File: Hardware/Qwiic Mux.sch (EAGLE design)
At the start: 62 parts, among them J2 SMD, J3 SMD, U2 PCA9548A

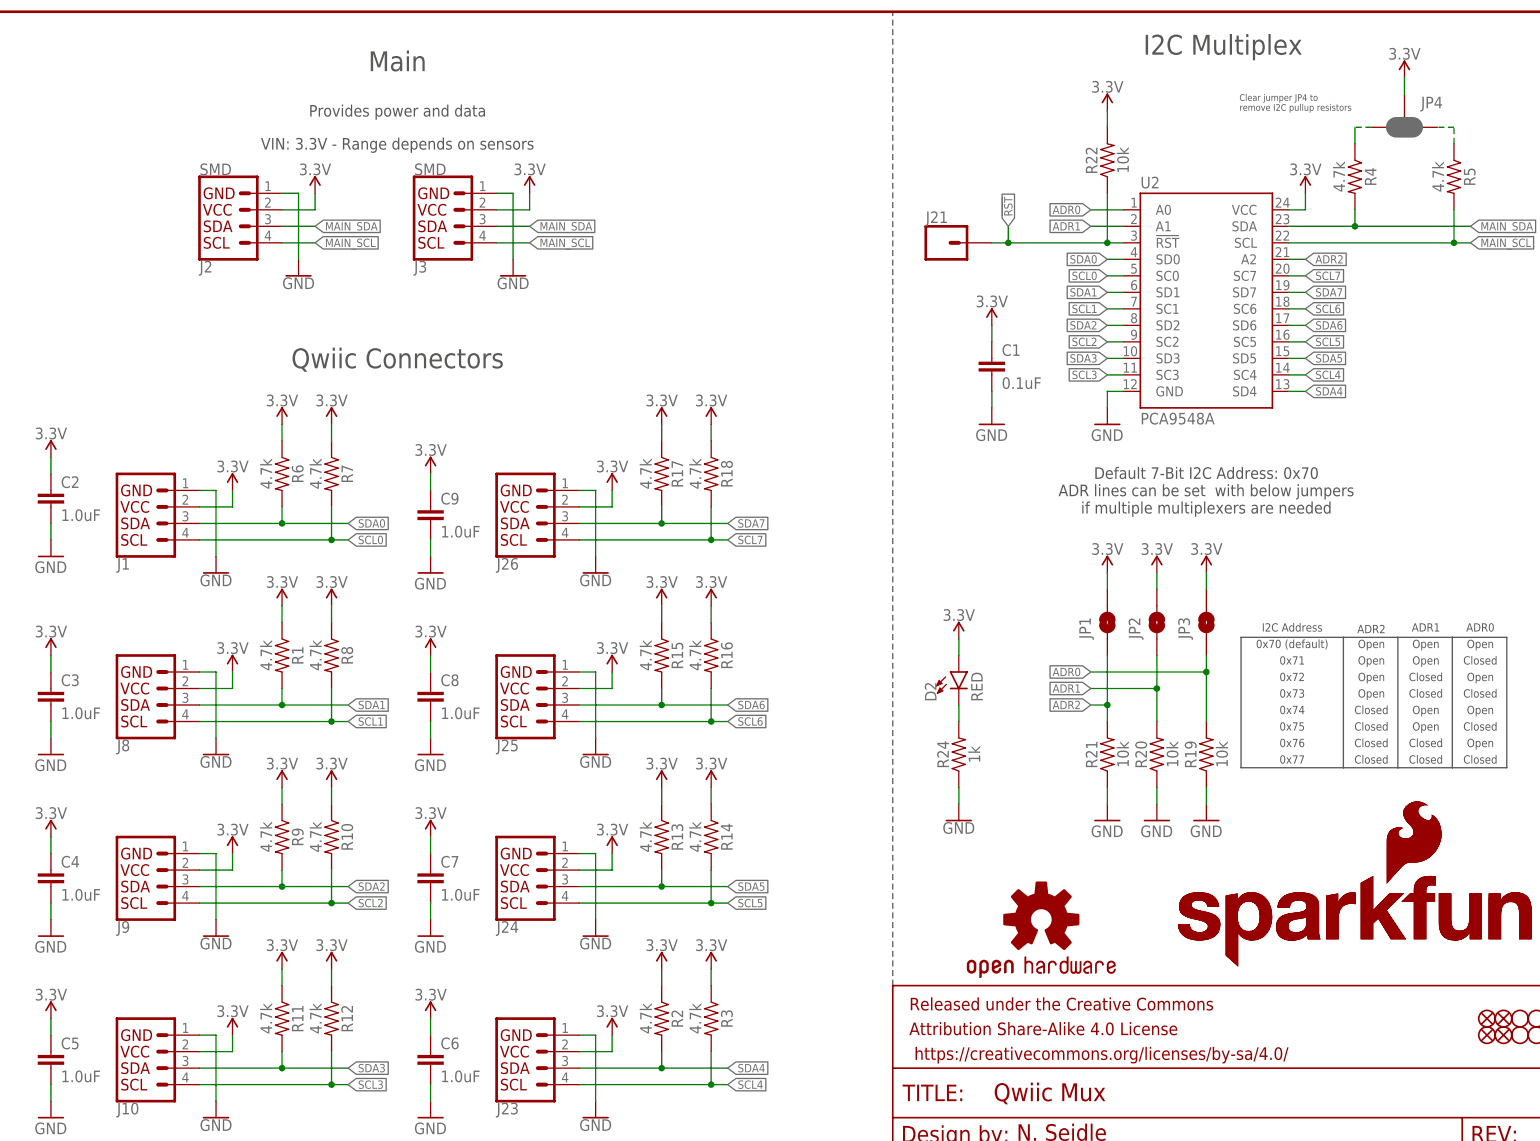
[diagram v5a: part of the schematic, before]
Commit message: Update Qwiic label. Update labels on ADR and RESET pins.
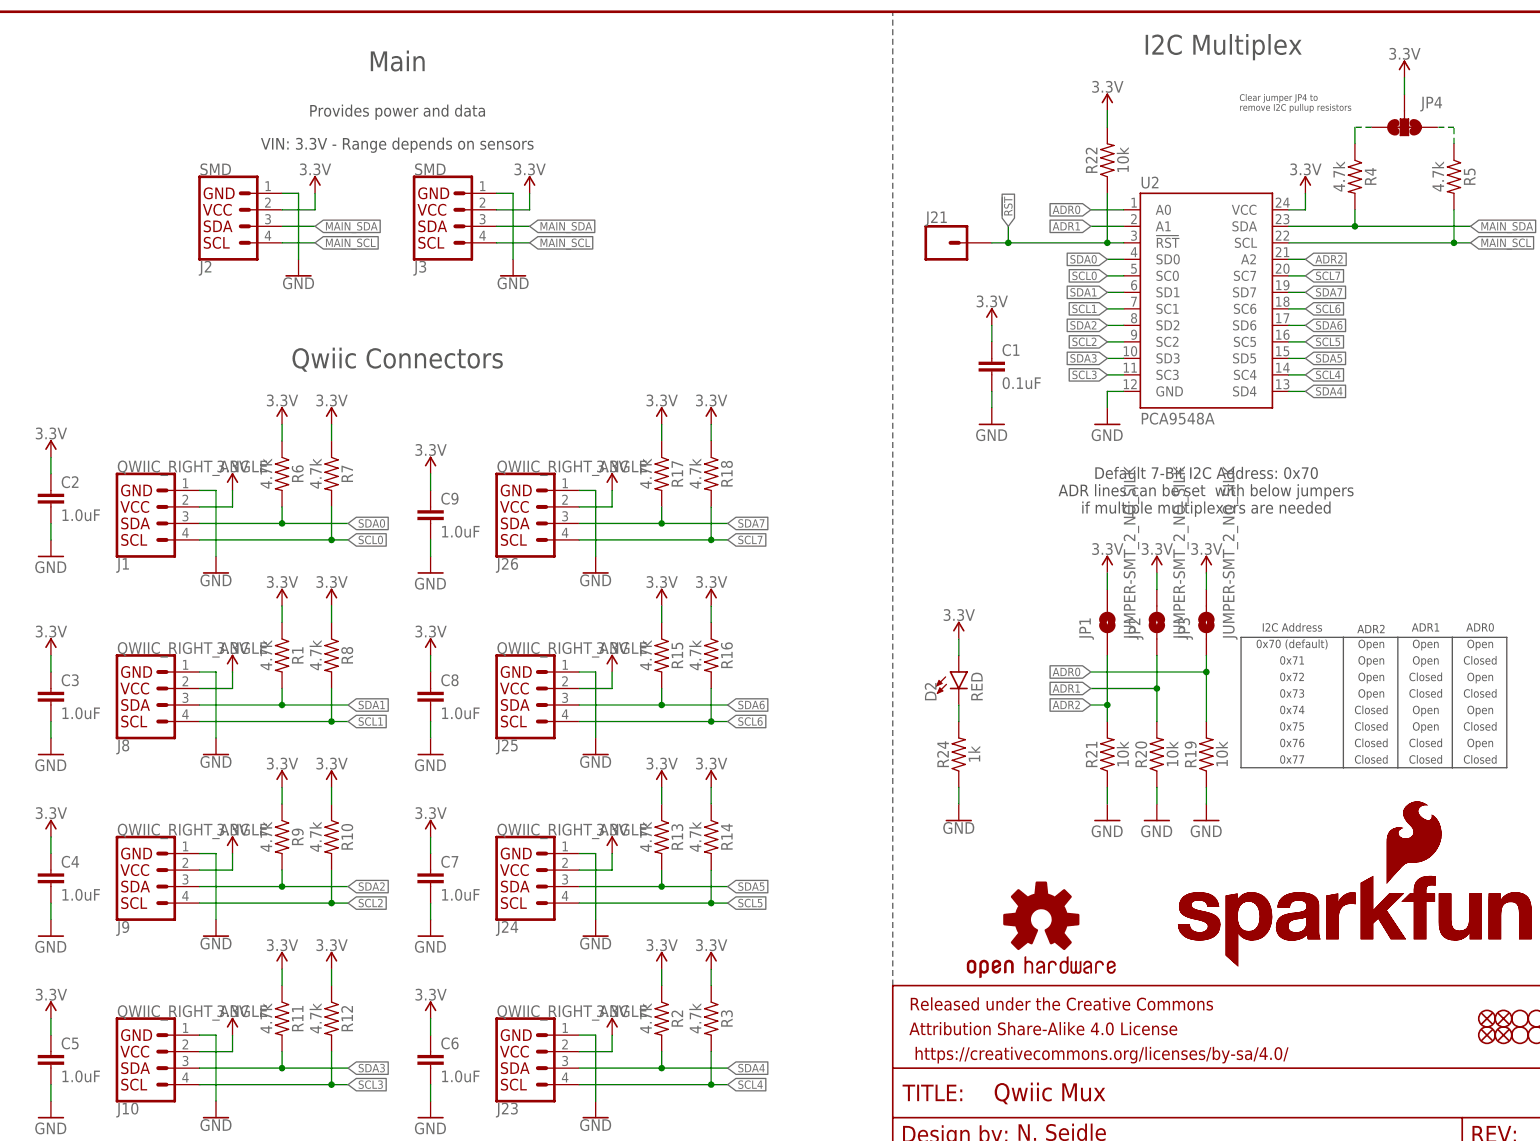
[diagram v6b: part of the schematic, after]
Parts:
- J1, J10, J23, J24, J25, J26, J8, J9: value (none) -> QWIIC_RIGHT_ANGLE
- JP4: value JUMPER-SMT_3_2-NC_PASTE_NO-SILK -> JUMPER-SMT_3_2-NC_TRACE_SILK; device SparkFun-Jumpers:JUMPER-SMT_3_2-NC_PASTE_NO-SILK -> SparkFun-Jumpers:JUMPER-SMT_3_2-NC_TRACE_SILK
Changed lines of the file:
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@@
 <?xml version="1.0" encoding="utf-8"?>
 <!DOCTYPE eagle SYSTEM "eagle.dtd">
-<eagle version="9.5.2">
+<eagle version="9.6.0">
 <drawing>
 <settings>
-<setting alwaysvectorfont="no"/>
+<setting alwaysvectorfont="yes"/>
 <setting keepoldvectorfont="yes"/>
 <setting verticaltext="up"/>
@@
 <layer number="115" name="ReferenceISLANDS" color="7" fill="1" visible="yes" active="yes"/>
 <layer number="116" name="Patch_BOT" color="9" fill="4" visible="yes" active="yes"/>
+<layer number="117" name="PM_Ref" color="26" fill="1" visible="no" active="no"/>
 <layer number="118" name="Rect_Pads" color="7" fill="1" visible="yes" active="yes"/>
+<layer number="119" name="PF_Ref" color="31" fill="1" visible="no" active="no"/>
+<layer number="120" name="WFL_Ref" color="25" fill="1" visible="no" active="no"/>
 <layer number="121" name="_tsilk" color="7" fill="1" visible="yes" active="yes"/>
 <layer number="122" name="_bsilk" color="7" fill="1" visible="yes" active="yes"/>
@@
 <part name="FD1" library="SparkFun-Aesthetics" deviceset="FIDUCIAL" device="1X2"/>
 <part name="FD2" library="SparkFun-Aesthetics" deviceset="FIDUCIAL" device="1X2"/>
-<part name="J1" library="SparkFun-Connectors" deviceset="QWIIC_CONNECTOR" device="JS-1MM"/>
+<part name="J1" library="SparkFun-Connectors" deviceset="QWIIC_CONNECTOR" device="JS-1MM" value="QWIIC_RIGHT_ANGLE"/>
 <part name="SUPPLY5" library="SparkFun-PowerSymbols" deviceset="3.3V" device=""/>
 <part name="GND2" library="SparkFun-PowerSymbols" deviceset="GND" device=""/>
-<part name="J8" library="SparkFun-Connectors" deviceset="QWIIC_CONNECTOR" device="JS-1MM"/>
+<part name="J8" library="SparkFun-Connectors" deviceset="QWIIC_CONNECTOR" device="JS-1MM" value="QWIIC_RIGHT_ANGLE"/>
 <part name="SUPPLY3" library="SparkFun-PowerSymbols" deviceset="3.3V" device=""/>
 <part name="GND5" library="SparkFun-PowerSymbols" deviceset="GND" device=""/>
-<part name="J9" library="SparkFun-Connectors" deviceset="QWIIC_CONNECTOR" device="JS-1MM"/>
+<part name="J9" library="SparkFun-Connectors" deviceset="QWIIC_CONNECTOR" device="JS-1MM" value="QWIIC_RIGHT_ANGLE"/>
 <part name="GND6" library="SparkFun-PowerSymbols" deviceset="GND" device=""/>
-<part name="J10" library="SparkFun-Connectors" deviceset="QWIIC_CONNECTOR" device="JS-1MM"/>
+<part name="J10" library="SparkFun-Connectors" deviceset="QWIIC_CONNECTOR" device="JS-1MM" value="QWIIC_RIGHT_ANGLE"/>
 <part name="GND7" library="SparkFun-PowerSymbols" deviceset="GND" device=""/>
 <part name="U$1" library="SparkFun-Aesthetics" deviceset="SFE_LOGO_NAME_FLAME" device=".1_INCH"/>
@@
 <part name="R11" library="SparkFun-Resistors" deviceset="4.7KOHM" device="-0603-1/10W-1%" value="4.7k"/>
 <part name="R12" library="SparkFun-Resistors" deviceset="4.7KOHM" device="-0603-1/10W-1%" value="4.7k"/>
-<part name="J23" library="SparkFun-Connectors" deviceset="QWIIC_CONNECTOR" device="JS-1MM"/>
+<part name="J23" library="SparkFun-Connectors" deviceset="QWIIC_CONNECTOR" device="JS-1MM" value="QWIIC_RIGHT_ANGLE"/>
 <part name="GND9" library="SparkFun-PowerSymbols" deviceset="GND" device=""/>
-<part name="J24" library="SparkFun-Connectors" deviceset="QWIIC_CONNECTOR" device="JS-1MM"/>
+<part name="J24" library="SparkFun-Connectors" deviceset="QWIIC_CONNECTOR" device="JS-1MM" value="QWIIC_RIGHT_ANGLE"/>
 <part name="GND10" library="SparkFun-PowerSymbols" deviceset="GND" device=""/>
-<part name="J25" library="SparkFun-Connectors" deviceset="QWIIC_CONNECTOR" device="JS-1MM"/>
+<part name="J25" library="SparkFun-Connectors" deviceset="QWIIC_CONNECTOR" device="JS-1MM" value="QWIIC_RIGHT_ANGLE"/>
 <part name="GND11" library="SparkFun-PowerSymbols" deviceset="GND" device=""/>
-<part name="J26" library="SparkFun-Connectors" deviceset="QWIIC_CONNECTOR" device="JS-1MM"/>
+<part name="J26" library="SparkFun-Connectors" deviceset="QWIIC_CONNECTOR" device="JS-1MM" value="QWIIC_RIGHT_ANGLE"/>
 <part name="GND12" library="SparkFun-PowerSymbols" deviceset="GND" device=""/>
 <part name="R2" library="SparkFun-Resistors" deviceset="4.7KOHM" device="-0603-1/10W-1%" value="4.7k"/>
@@
 <part name="GND14" library="SparkFun" deviceset="GND" device=""/>
 <part name="GND15" library="SparkFun" deviceset="GND" device=""/>
-<part name="JP1" library="SparkFun-Jumpers" deviceset="JUMPER-SMT_2_NO" device="_SILK" value=""/>
-<part name="JP2" library="SparkFun-Jumpers" deviceset="JUMPER-SMT_2_NO" device="_SILK" value=""/>
-<part name="JP3" library="SparkFun-Jumpers" deviceset="JUMPER-SMT_2_NO" device="_SILK" value=""/>
+<part name="JP1" library="SparkFun-Jumpers" deviceset="JUMPER-SMT_2_NO" device="_SILK" package3d_urn="urn:adsk.eagle:package:39279/1" value="JUMPER-SMT_2_NO_SILK"/>
+<part name="JP2" library="SparkFun-Jumpers" deviceset="JUMPER-SMT_2_NO" device="_SILK" package3d_urn="urn:adsk.eagle:package:39279/1" value="JUMPER-SMT_2_NO_SILK"/>
+<part name="JP3" library="SparkFun-Jumpers" deviceset="JUMPER-SMT_2_NO" device="_SILK" package3d_urn="urn:adsk.eagle:package:39279/1" value="JUMPER-SMT_2_NO_SILK"/>
 <part name="SUPPLY32" library="SparkFun-PowerSymbols" deviceset="3.3V" device=""/>
 <part name="SUPPLY33" library="SparkFun-PowerSymbols" deviceset="3.3V" device=""/>
@@
 <part name="FD4" library="SparkFun-Aesthetics" deviceset="FIDUCIAL" device="1X2"/>
 <part name="SUPPLY2" library="SparkFun-PowerSymbols" deviceset="3.3V" device=""/>
-<part name="JP4" library="SparkFun-Jumpers" deviceset="JUMPER-SMT_3_2-NC_PASTE" device="_NO-SILK"/>
+<part name="JP4" library="SparkFun-Jumpers" deviceset="JUMPER-SMT_3_2-NC_TRACE" device="_SILK" package3d_urn="urn:adsk.eagle:package:39289/1"/>
 <part name="SUPPLY1" library="SparkFun-PowerSymbols" deviceset="3.3V" device=""/>
 <part name="J3" library="SparkX" deviceset="I2C_STANDARD" device="JS-1MM" value="SMD"/>
@@
 which will not be processed correctly with this version.
 </note>
+<note version="8.3" severity="warning">
+Since Version 8.3, EAGLE supports URNs for individual library
+assets (packages, symbols, and devices). The URNs of those assets
+will not be understood (or retained) with this version.
+</note>
+<note version="8.3" severity="warning">
+Since Version 8.3, EAGLE supports the association of 3D packages
+with devices in libraries, schematics, and board files. Those 3D
+packages will not be understood (or retained) with this version.
+</note>
 </compatibility>
